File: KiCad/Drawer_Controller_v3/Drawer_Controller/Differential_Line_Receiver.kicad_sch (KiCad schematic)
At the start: 6 parts, among them U15 SN75176BDR, U16 SN75176BDR, U17 SN75176BDR

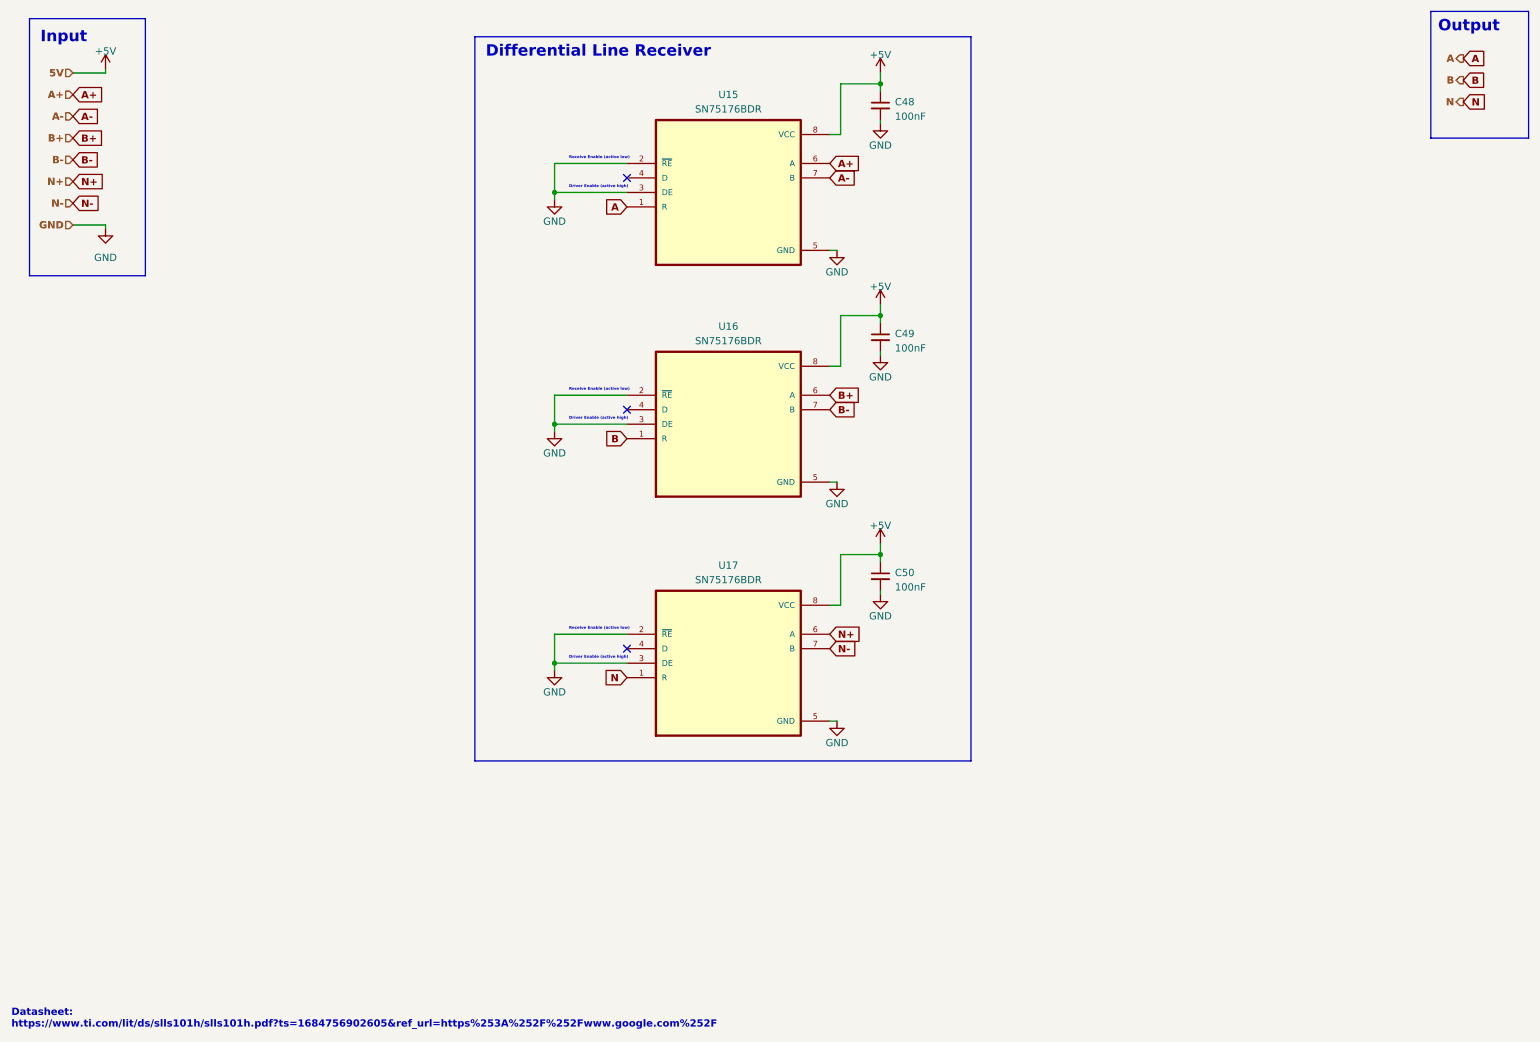
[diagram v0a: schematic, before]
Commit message: Fixing some ERC errors and warnings
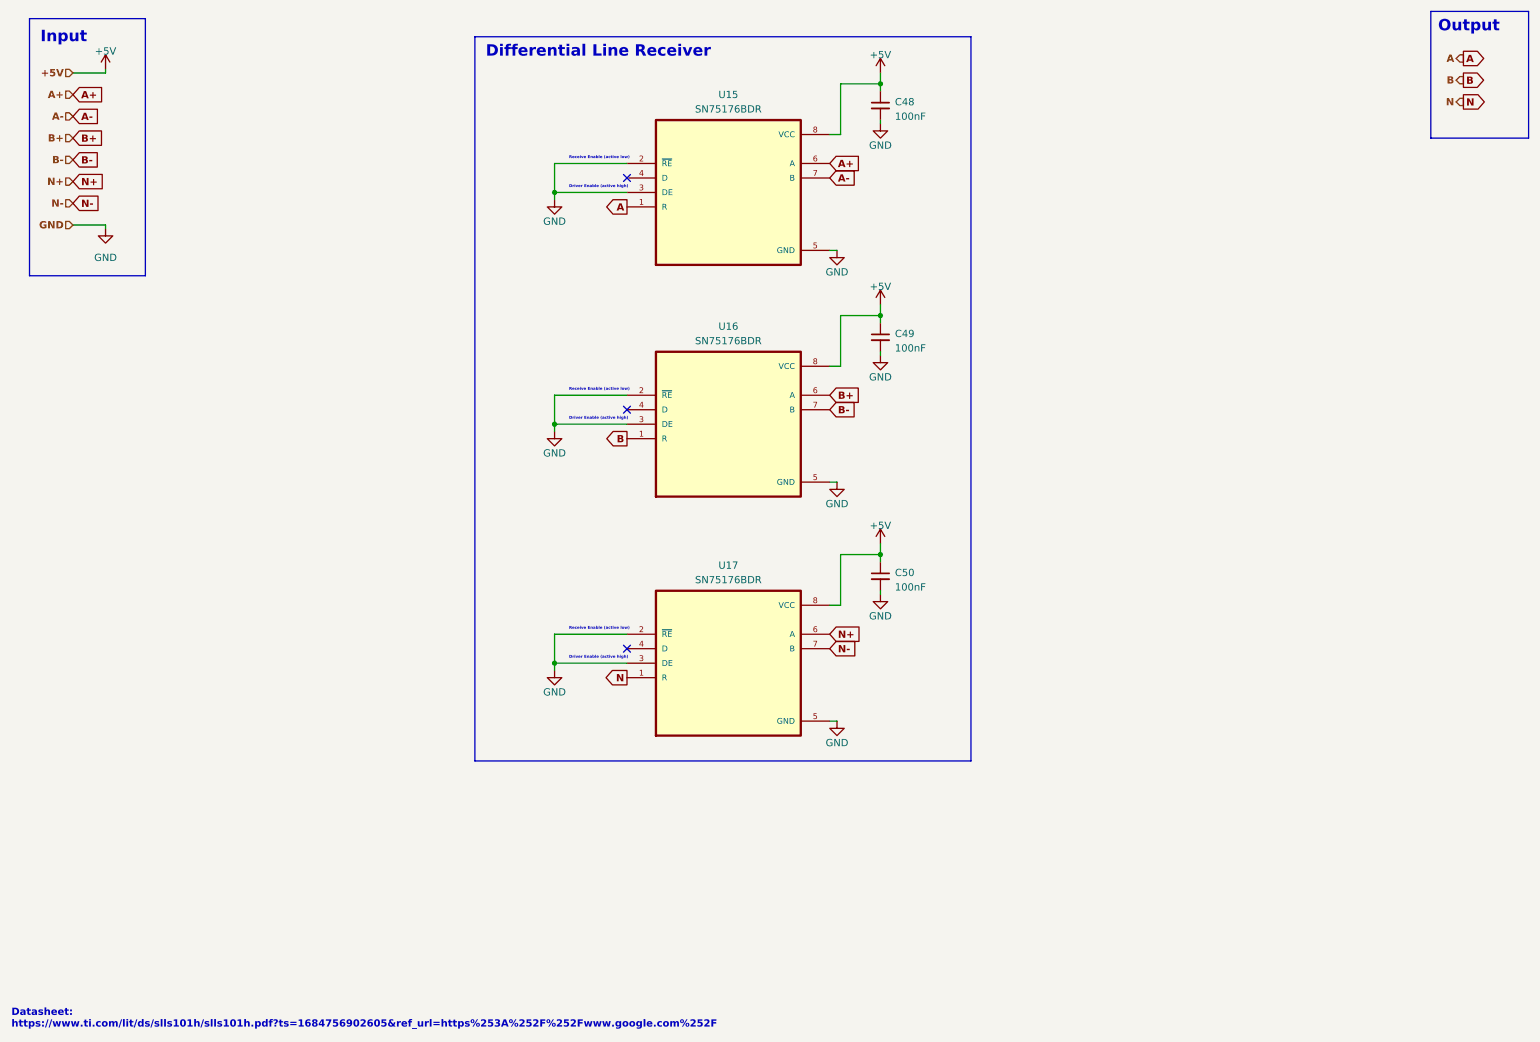
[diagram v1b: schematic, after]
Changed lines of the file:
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@@
     (effects (font (size 0.5 0.5) bold) (justify left bottom))
   )
-  (global_label "B" (shape input) (at 123.19 90.805 180) (fields_autoplaced)
+  (global_label "B" (shape output) (at 123.19 90.805 180) (fields_autoplaced)
     (effects (font (size 1.27 1.27) bold) (justify right))
     (property "Intersheetrefs" "${INTERSHEET_REFS}" (at 118.5858 90.805 0)
@@
     )
   )
-  (global_label "N" (shape input) (at 269.875 31.75 0) (fields_autoplaced)
+  (global_label "N" (shape output) (at 269.875 31.75 0) (fields_autoplaced)
     (effects (font (size 1.27 1.27) bold) (justify left))
     (property "Intersheetrefs" "${INTERSHEET_REFS}" (at 274.5397 31.75 0)
@@
     )
   )
-  (global_label "N" (shape input) (at 123.19 132.715 180) (fields_autoplaced)
+  (global_label "N" (shape output) (at 123.19 132.715 180) (fields_autoplaced)
     (effects (font (size 1.27 1.27) bold) (justify right))
     (property "Intersheetrefs" "${INTERSHEET_REFS}" (at 118.5253 132.715 0)
@@
     )
   )
-  (global_label "B" (shape input) (at 269.875 27.94 0) (fields_autoplaced)
+  (global_label "B" (shape output) (at 269.875 27.94 0) (fields_autoplaced)
     (effects (font (size 1.27 1.27) bold) (justify left))
     (property "Intersheetrefs" "${INTERSHEET_REFS}" (at 274.4792 27.94 0)
@@
     )
   )
-  (global_label "A" (shape input) (at 123.19 50.165 180) (fields_autoplaced)
+  (global_label "A" (shape output) (at 123.19 50.165 180) (fields_autoplaced)
     (effects (font (size 1.27 1.27) bold) (justify right))
     (property "Intersheetrefs" "${INTERSHEET_REFS}" (at 118.7672 50.165 0)
@@
     )
   )
-  (global_label "A" (shape input) (at 269.875 24.13 0) (fields_autoplaced)
+  (global_label "A" (shape output) (at 269.875 24.13 0) (fields_autoplaced)
     (effects (font (size 1.27 1.27) bold) (justify left))
     (property "Intersheetrefs" "${INTERSHEET_REFS}" (at 274.2978 24.13 0)
@@
     (effects (font (size 1.27 1.27) bold) (justify right))
   )
-  (hierarchical_label "5V" (shape input) (at 26.035 26.67 180) (fields_autoplaced)
+  (hierarchical_label "+5V" (shape input) (at 26.035 26.67 180) (fields_autoplaced)
     (effects (font (size 1.27 1.27) bold) (justify right))
   )

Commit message: Finished assigning all footprints
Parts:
- C48, C49, C50: footprint (none) -> Capacitor_SMD:C_0402_1005Metric
- U15, U16, U17: footprint SOIC127P599X175-8N -> Robast_Footprints:SN75176BDR
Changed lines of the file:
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@@
       (effects (font (size 1.27 1.27)) (justify left))
     )
-    (property "Footprint" "" (at 167.64 114.935 0)
+    (property "Footprint" "Capacitor_SMD:C_0402_1005Metric" (at 167.64 114.935 0)
       (effects (font (size 1.27 1.27)) hide)
     )
@@
       (effects (font (size 1.27 1.27)))
     )
-    (property "Footprint" "SOIC127P599X175-8N" (at 140.97 47.625 0)
+    (property "Footprint" "Robast_Footprints:SN75176BDR" (at 140.97 47.625 0)
       (effects (font (size 1.27 1.27)) (justify bottom) hide)
     )
@@
       (effects (font (size 1.27 1.27)))
     )
-    (property "Footprint" "SOIC127P599X175-8N" (at 140.97 130.175 0)
+    (property "Footprint" "Robast_Footprints:SN75176BDR" (at 140.97 130.175 0)
       (effects (font (size 1.27 1.27)) (justify bottom) hide)
     )
@@
       (effects (font (size 1.27 1.27)) (justify left))
     )
-    (property "Footprint" "" (at 167.64 73.025 0)
+    (property "Footprint" "Capacitor_SMD:C_0402_1005Metric" (at 167.64 73.025 0)
       (effects (font (size 1.27 1.27)) hide)
     )
@@
       (effects (font (size 1.27 1.27)) (justify left))
     )
-    (property "Footprint" "" (at 167.64 32.385 0)
+    (property "Footprint" "Capacitor_SMD:C_0402_1005Metric" (at 167.64 32.385 0)
       (effects (font (size 1.27 1.27)) hide)
     )
@@
       (effects (font (size 1.27 1.27)))
     )
-    (property "Footprint" "SOIC127P599X175-8N" (at 140.97 88.265 0)
+    (property "Footprint" "Robast_Footprints:SN75176BDR" (at 140.97 88.265 0)
       (effects (font (size 1.27 1.27)) (justify bottom) hide)
     )
